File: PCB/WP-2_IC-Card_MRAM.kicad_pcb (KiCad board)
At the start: 2 copper layers, 54 x 54 mm, 38 parts, among them J1 SMS-138-01-G-S, SW1 CUS-14TB, U1 MRxA08xxYSxxx, U2 MIC5317-3.3YD5, U3 4245, U4 4245, U5 4245, U6 4245

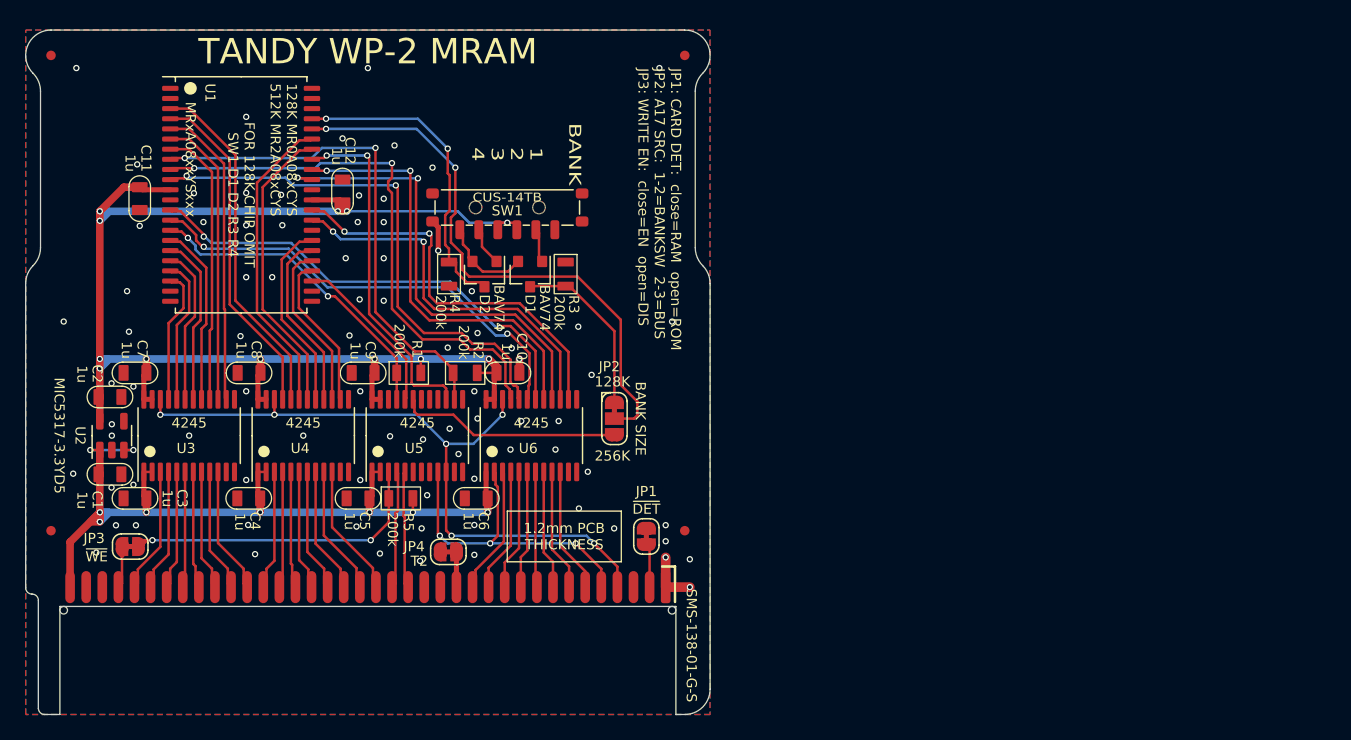
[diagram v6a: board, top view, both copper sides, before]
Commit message: silkscreens, board outlines, switch slider, covers fitment, copper to edge
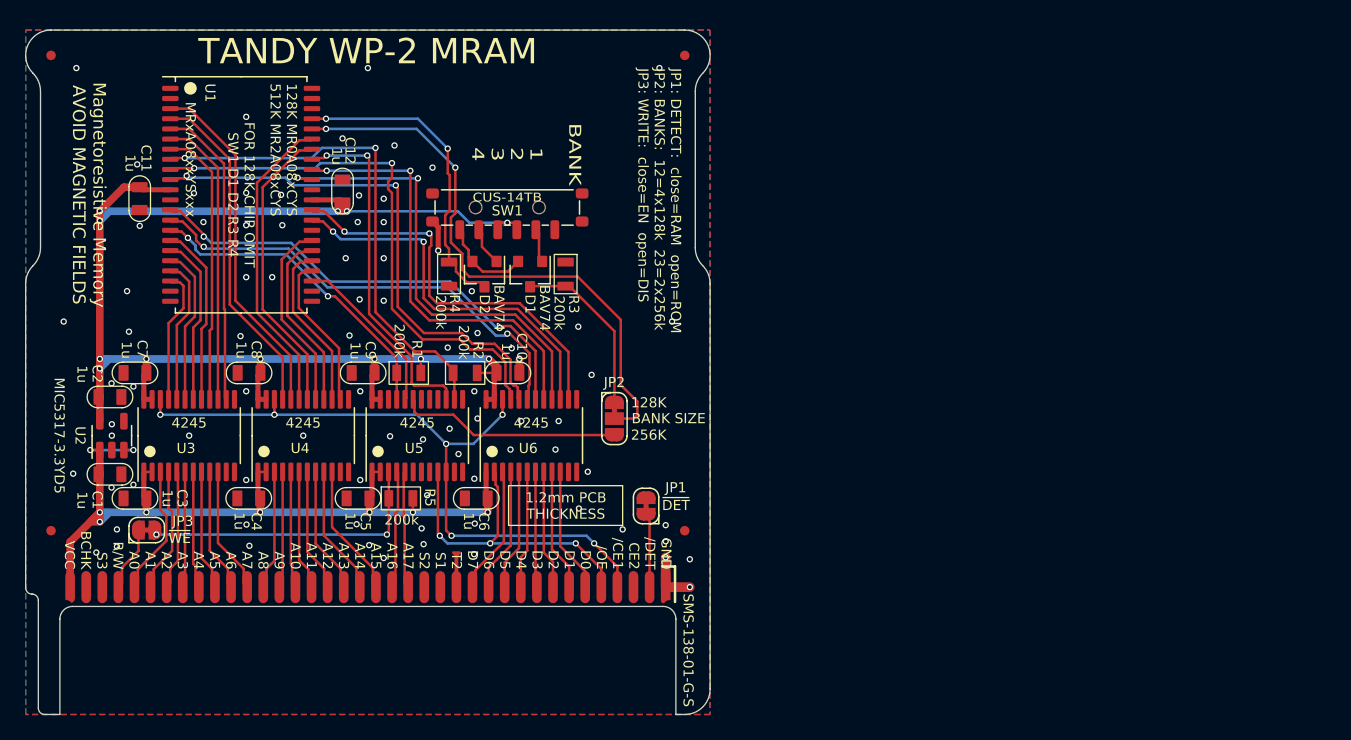
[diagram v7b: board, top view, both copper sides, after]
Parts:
- removed JP4: T2, 000_LOCAL:SolderJumper-2_Bridged
- removed the REF** at (112.0, 114.0)
- removed the REF** at (159.9, 114.0)
- J1: footprint 000_LOCAL:SMS-138-01-x-x_pcb_edge -> 000_LOCAL:SMS-138-01-x-S_pcb_edge
- N1: value WP-2_IC-Card_Cover_MRAM -> WP-2_IC_Card_Cover_MRAM_512
- moved JP1 2.40 mm to (157.9, 105.8)
- moved JP3 1.84 mm to (118.5, 107.7)
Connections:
- J1 pad 14: /T2 -> GND
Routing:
- net /T2: track 2.78 -> 0.00 mm
- net GND: track 7.84 -> 10.3 mm, vias 83 -> 84
- net /~{DET}: track 3.45 -> 5.86 mm
- net /R/~{W}: track 3.32 -> 5.16 mm
- net /~{WE}: track 24.5 -> 23.6 mm
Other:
- outline, holes or cut-outs redrawn
- board text added: "GND /DET CE2 /CE1 /OE D0 D1 D2 D3 D4 D5 D6 D7 T2 S1 S2 A17 A16 A15 A14 A13 A12 A11 A10 A9 A8 A7 A6 A5 A4 A3 A2 A1 A0 R/W S3 BCHK VCC"
- board text added: "JP1: DETECT: close=RAM open=ROM JP2: BANKS: 12=4x128k 23=2x256k JP3: WRITE: close=EN open=DIS"
- board text added: "Magnetoresistive Memory AVOID MAGNETIC FIELDS"
- board text removed: "BOARD OUTLINE"
- board text removed: "JP1: CARD DET: close=RAM open=ROM JP2: A17 SRC: 1-2=BANKSW 2-3=BUS JP3: WRITE EN: close=EN open=DIS"

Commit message: restore mram cover component pocket outline
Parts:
- JP2: value BANK SIZE -> RAM_A17
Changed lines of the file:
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@@
 	(title_block
 		(title "WP-2_IC-Card_MRAM")
-		(date "2025-10-30")
-		(rev "031")
+		(date "2025-11-02")
+		(rev "032")
 		(company "Brian K. White - b.kenyon.w@gmail.com")
 		(comment 1 "CC-BY-SA")
@@
 		)
 		(fp_line
+			(start -22.5 11.1)
+			(end -22.5 -0.9)
+			(stroke
+				(width 0.05)
+				(type default)
+			)
+			(layer "F.Fab")
+		)
+		(fp_line
+			(start -22 -1.4)
+			(end 22 -1.4)
+			(stroke
+				(width 0.05)
+				(type default)
+			)
+			(layer "F.Fab")
+		)
+		(fp_line
 			(start -0.25 0)
 			(end 0.25 0)
@@
 			(layer "F.Fab")
 		)
+		(fp_line
+			(start 22 11.6)
+			(end -22 11.6)
+			(stroke
+				(width 0.05)
+				(type default)
+			)
+			(layer "F.Fab")
+		)
+		(fp_line
+			(start 22.5 -0.9)
+			(end 22.5 11.1)
+			(stroke
+				(width 0.05)
+				(type default)
+			)
+			(layer "F.Fab")
+		)
+		(fp_arc
+			(start -22.500001 -0.9)
+			(mid -22.353554 -1.253553)
+			(end -22.000001 -1.4)
+			(stroke
+				(width 0.05)
+				(type default)
+			)
+			(layer "F.Fab")
+		)
+		(fp_arc
+			(start -22.000001 11.6)
+			(mid -22.353554 11.453554)
+			(end -22.5 11.100001)
+			(stroke
+				(width 0.05)
+				(type default)
+			)
+			(layer "F.Fab")
+		)
+		(fp_arc
+			(start 22.000001 -1.399999)
+			(mid 22.353554 -1.253553)
+			(end 22.5 -0.9)
+			(stroke
+				(width 0.05)
+				(type default)
+			)
+			(layer "F.Fab")
+		)
+		(fp_arc
+			(start 22.5 11.100001)
+			(mid 22.353554 11.453554)
+			(end 22.000001 11.6)
+			(stroke
+				(width 0.05)
+				(type default)
+			)
+			(layer "F.Fab")
+		)
 		(fp_circle
 			(center 0 0)
@@
 			)
 		)
-		(property "Value" "BANK SIZE"
+		(property "Value" "RAM_A17"
 			(at -0.005 -1.35 0)
 			(unlocked yes)
@@
 			)
 		)
-		(property "Label_1-2" "128K"
+		(property "Label_1-2" "BANKSW"
 			(at -1.255 -1.3 0)
 			(unlocked yes)
@@
 			)
 		)
-		(property "Label_2-3" "256K"
+		(property "Label_2-3" "BUS_A17"
 			(at 1.295 -1.3 0)
 			(unlocked yes)
@@
 	)
 	(zone
-		(net 72)
-		(net_name "/3A17")
+		(net 91)
+		(net_name "/3A17bus")
 		(layer "F.Cu")
 		(name "$teardrop_padvia$")
 		(hatch none 0.1)
-		(priority 30014)
+		(priority 30001)
 		(attr
 			(teardrop
@@
 		(polygon
 			(pts
-				(xy 156.65 98.8) (xy 156.529649 98.780468) (xy 156.450534 98.752407) (xy 156.370757 98.712711) (xy 156.302033 98.666801)
-				(xy 156.241449 98.612046) (xy 156.200598 98.560593) (xy 156.170396 98.503636) (xy 156.155306 98.453499)
-				(xy 156.15 98.4) (xy 155.399 98.9) (xy 156.15 99.4) (xy 156.168572 99.300988) (xy 156.224128 99.207679)
-				(xy 156.319547 99.120209) (xy 156.453657 99.046282) (xy 156.602516 99.003647) (xy 156.65 99)
+				(xy 154.404278 100.3) (xy 154.489286 100.306291) (xy 154.589645 100.330328) (xy 154.645185 100.356232)
+				(xy 154.69039 100.392795) (xy 154.721926 100.45) (xy 155.401 100.2) (xy 154.65 99.95) (xy 154.645834 99.983695)
+				(xy 154.633124 100.012131) (xy 154.583601 100.057723) (xy 154.497954 100.089448) (xy 154.404278 100.1)
 			)
 		)
@@
 	)
 	(zone
-		(net 91)
-		(net_name "/3A17bus")
-		(layer "F.Cu")
-		(name "$teardrop_padvia$")
-		(hatch none 0.1)
-		(priority 30080)
-		(attr
-			(teardrop
-				(type padvia)
-			)
-		)
-		(connect_pads yes
-			(clearance 0)
-		)
-		(min_thickness 0.0254)
-		(filled_areas_thickness no)
-		(fill yes
-			(thermal_gap 0.5)
-			(thermal_bridge_width 0.5)
-			(island_removal_mode 1)
-			(island_area_min 10)
-		)
-		(polygon
-			(pts
-				(xy 154.404278 100.3) (xy 154.489286 100.306291) (xy 154.589645 100.330328) (xy 154.645185 100.356232)
-				(xy 154.69039 100.392795) (xy 154.721926 100.45) (xy 155.401 100.2) (xy 154.65 99.95) (xy 154.645834 99.983695)
-				(xy 154.633124 100.012131) (xy 154.583601 100.057723) (xy 154.497954 100.089448) (xy 154.404278 100.1)
-			)
-		)
-	)
-	(zone
 		(net 2)
 		(net_name "/~{CE1}")
@@
 	)
 	(zone
-		(net 29)
-		(net_name "/3A17bank")
-		(layer "F.Cu")
-		(name "$teardrop_padvia$")
-		(hatch none 0.1)
-		(priority 30159)
-		(attr
-			(teardrop
-				(type padvia)
-			)
-		)
-		(connect_pads yes
-			(clearance 0)
-		)
-		(min_thickness 0.0254)
-		(filled_areas_thickness no)
-		(fill yes
-			(thermal_gap 0.5)
-			(thermal_bridge_width 0.5)
-			(island_removal_mode 1)
-			(island_area_min 10)
-		)
-		(polygon
-			(pts
-				(xy 155.3 96.85) (xy 155.293709 96.92246) (xy 155.269672 97.007555) (xy 155.244646 97.051119) (xy 155.209604 97.083583)
-				(xy 155.15 97.1) (xy 155.4 97.601) (xy 155.65 97.1) (xy 155.616377 97.095257) (xy 155.58799 97.082055)
-				(xy 155.542297 97.031444) (xy 155.510514 96.944513) (xy 155.5 96.85)
-			)
-		)
-	)
-	(zone
 		(net 2)
 		(net_name "/~{CE1}")
@@
 	)
 	(zone
+		(net 72)
+		(net_name "/3A17")
+		(layer "F.Cu")
+		(name "$teardrop_padvia$")
+		(hatch none 0.1)
+		(priority 30000)
+		(attr
+			(teardrop
+				(type padvia)
+			)
+		)
+		(connect_pads yes
+			(clearance 0)
+		)
+		(min_thickness 0.0254)
+		(filled_areas_thickness no)
+		(fill yes
+			(thermal_gap 0.5)
+			(thermal_bridge_width 0.5)
+			(island_removal_mode 1)
+			(island_area_min 10)
+		)
+		(polygon
+			(pts
+				(xy 156.65 98.8) (xy 156.529649 98.780468) (xy 156.450534 98.752407) (xy 156.370757 98.712711) (xy 156.302033 98.666801)
+				(xy 156.241449 98.612046) (xy 156.200598 98.560593) (xy 156.170396 98.503636) (xy 156.155306 98.453499)
+				(xy 156.15 98.4) (xy 155.399 98.9) (xy 156.15 99.4) (xy 156.168572 99.300988) (xy 156.224128 99.207679)
+				(xy 156.319547 99.120209) (xy 156.453657 99.046282) (xy 156.602516 99.003647) (xy 156.65 99)
+			)
+		)
+	)
+	(zone
 		(net 8)
 		(net_name "/D4")
@@
 			)
 		)
+	)
+	(zone
+		(net 29)
+		(net_name "/3A17bank")
+		(layer "F.Cu")
+		(name "$teardrop_padvia$")
+		(hatch none 0.1)
+		(priority 30002)
+		(attr
+			(teardrop
+				(type padvia)
+			)
+		)
+		(connect_pads yes
+			(clearance 0)
+		)
+		(min_thickness 0.0254)
+		(filled_areas_thickness no)
+		(fill yes
+			(thermal_gap 0.5)
+			(thermal_bridge_width 0.5)
+			(island_removal_mode 1)
+			(island_area_min 10)
+		)
+		(polygon
+			(pts
+				(xy 155.3 96.85) (xy 155.293709 96.92246) (xy 155.269672 97.007555) (xy 155.244646 97.051119) (xy 155.209604 97.083583)
+				(xy 155.15 97.1) (xy 155.4 97.601) (xy 155.65 97.1) (xy 155.616377 97.095257) (xy 155.58799 97.082055)
+				(xy 155.542297 97.031444) (xy 155.510514 96.944513) (xy 155.5 96.85)
+			)
+		)
